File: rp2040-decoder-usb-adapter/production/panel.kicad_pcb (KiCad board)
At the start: 2 copper layers, 70 x 70 mm, 277 parts, among them J1 505070-2422, J2 SWD, J3 SPEAKER, J4 MISC1, J8 RAIL_PADS, P1 USB_C_Receptacle_USB2.0_16P

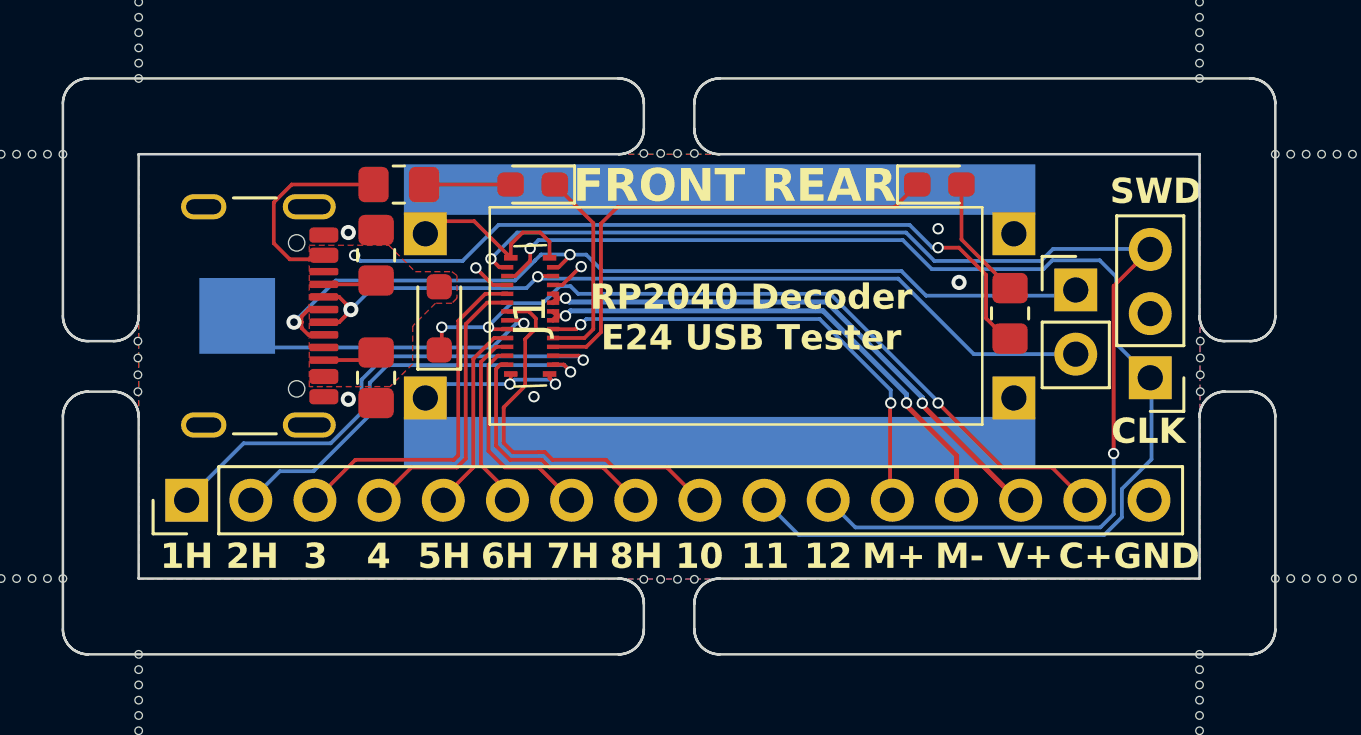
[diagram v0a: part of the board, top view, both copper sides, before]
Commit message: feat: move usb port to avoid shorting rails
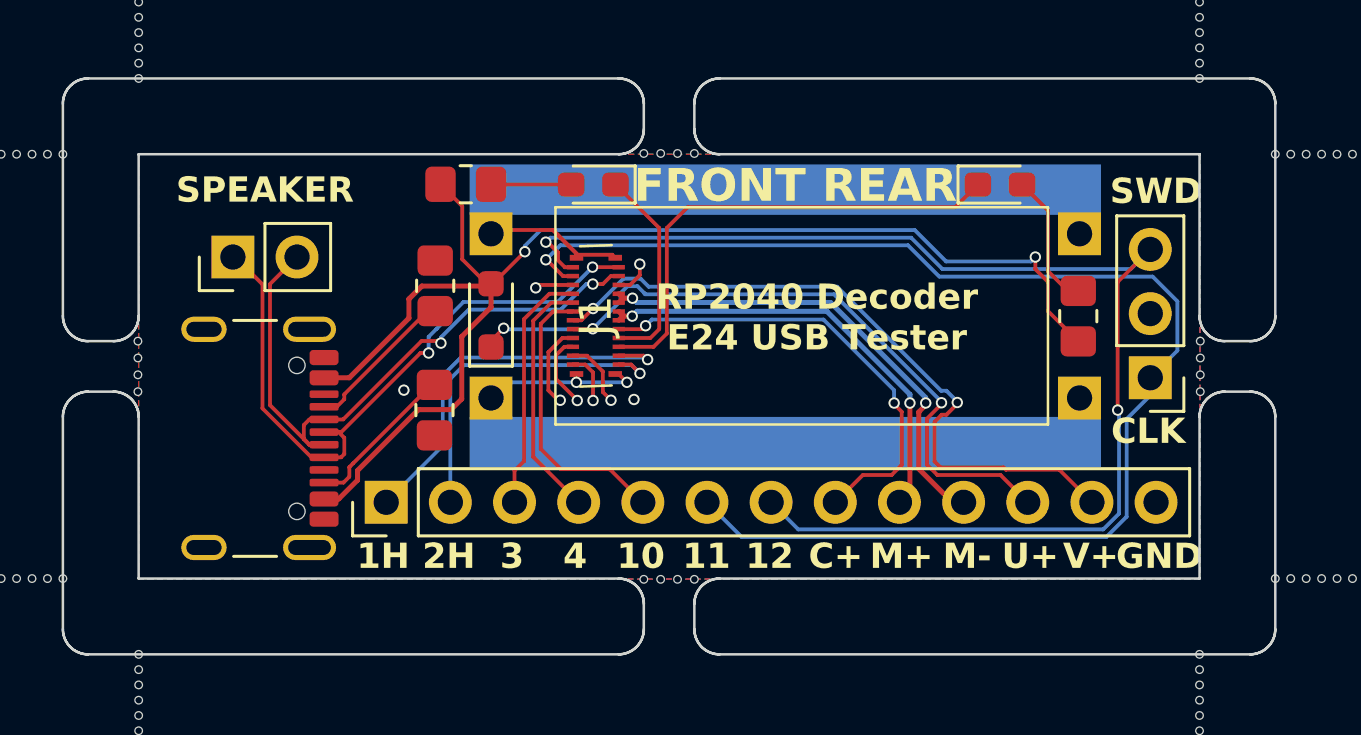
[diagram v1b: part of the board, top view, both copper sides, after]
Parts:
- removed TP1: VCC, TestPoint:TestPoint_Pad_3.0x3.0mm
- J4: footprint Connector_PinHeader_2.54mm:PinHeader_1x16_P2.54mm_Vertical -> Connector_PinHeader_2.54mm:PinHeader_1x13_P2.54mm_Vertical
- moved J3 33.4 mm to (131.2, 50.7), turned to 90 degrees
- moved J4 7.90 mm to (137.3, 60.4)
- moved P1 4.85 mm to (131.2, 57.9)
- moved R4 2.70 mm to (164.7, 53.0)
- moved R3 2.65 mm to (140.4, 47.8)
- moved R2 2.64 mm to (139.2, 56.7)
- moved R1 2.63 mm to (139.2, 51.8)
- moved J1 2.60 mm to (145.6, 53.0)
- moved J8 2.60 mm to (153.1, 53.0)
- moved D2 2.40 mm to (145.5, 47.8)
- moved D3 2.40 mm to (161.6, 47.8)
- moved D1 2.05 mm to (141.4, 53.0)
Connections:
- J4 pad 10: Board_0-/AUX11 -> Board_0-/MOTOR_B
- J4 pad 11: Board_0-/AUX12 -> Board_0-VDC
- J4 pad 12: Board_0-/CAP+ -> Board_0-VCC
- J4 pad 13: Board_0-/MOTOR_A -> Board_0-GND
- J4 pad 5: Board_0-/AUX5 (VDC) -> Board_0-/AUX10
- J4 pad 6: Board_0-/AUX6 (VDC) -> Board_0-/AUX11
- J4 pad 7: Board_0-/AUX7 (VDC) -> Board_0-/AUX12
- J4 pad 8: Board_0-/AUX8 (VDC) -> Board_0-/CAP+
- J4 pad 9: Board_0-/AUX10 -> Board_0-/MOTOR_A
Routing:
- net Board_0-+5V: track 37.7 -> 53.0 mm
- net Board_0-VCC: track 13.0 -> 27.7 mm, vias 1 -> 2
- net Board_0-/D+: track 36.5 -> 26.3 mm
- net Board_0-/D-: track 33.8 -> 25.7 mm
- net Board_0-/AUX8 (VDC): track 9.99 -> 2.04 mm, vias 0 -> 1
- net Board_0-/AUX7 (VDC): track 8.40 -> 2.72 mm, vias 0 -> 1
- net Board_0-/AUX1 (VDC): track 20.2 -> 15.6 mm
- net Board_0-/AUX5 (VDC): track 7.78 -> 3.35 mm, vias 0 -> 1
- net Board_0-/AUX3: track 14.1 -> 9.76 mm
- net Board_0-/AUX6 (VDC): track 7.20 -> 2.95 mm, vias 0 -> 1
- net Board_0-/AUX10: track 15.4 -> 11.3 mm
- net Board_0-Net-(P1-CC2): track 2.16 -> 6.20 mm
- net Board_0-Net-(P1-CC1): track 2.19 -> 6.08 mm
- net Board_0-/MOTOR_A: track 20.8 -> 17.7 mm
- net Board_0-/MOTOR_B: track 22.3 -> 19.4 mm
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- removed copper zone on F.Cu, net Board_0-+5V
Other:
- board text added: "SPEAKER"
- board text added: "U+"
- board text removed: "5H"
- board text removed: "6H"
- board text removed: "7H"
- board text removed: "8H"
